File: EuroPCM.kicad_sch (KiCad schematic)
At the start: 1 part, among them IC1 TDA1541A

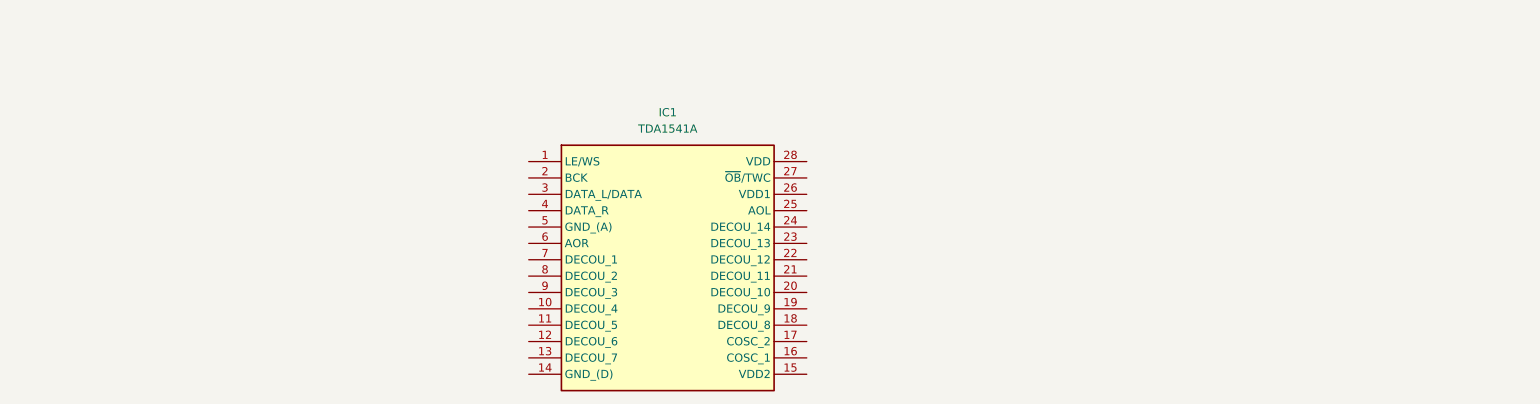
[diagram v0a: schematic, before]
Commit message: Add tda1315 footprint use schematic sheets
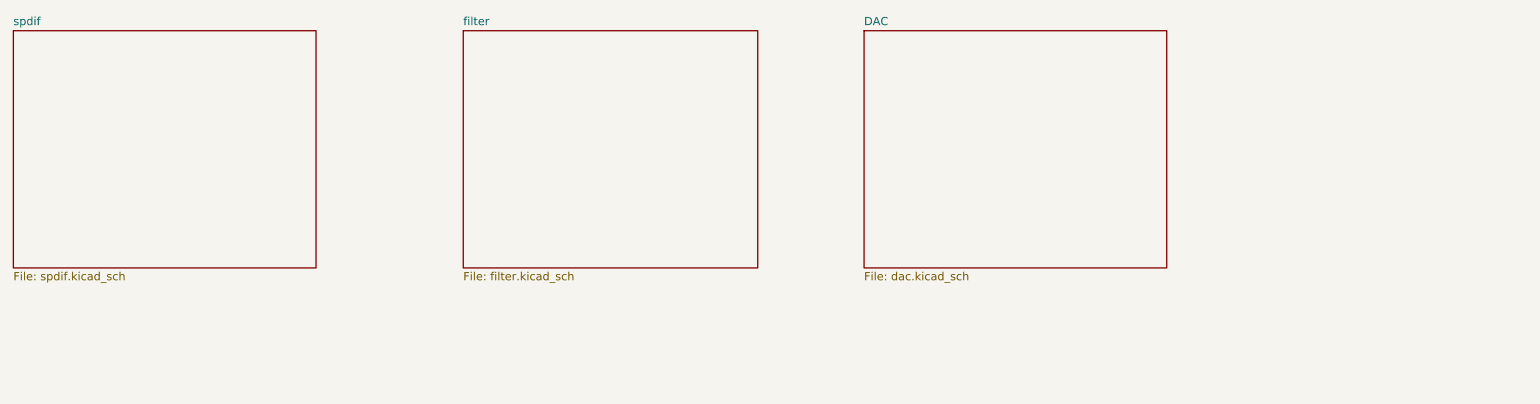
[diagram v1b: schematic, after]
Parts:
- removed IC1: TDA1541A, DIP1652W53P254L3550H510Q28N, symbol tda1541:TDA1541A
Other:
- added sheet DAC (dac.kicad_sch)
- added sheet filter (filter.kicad_sch)
- added sheet spdif (spdif.kicad_sch)
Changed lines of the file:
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@@
 	(generator_version "9.0")
 	(paper "A4")
-	(symbol
-		(lib_id "tda1541:TDA1541A")
-		(at 119.38 77.47 0)
-		(unit 1)
+	(sheet
+		(at 171.45 57.15)
+		(size 46.99 36.83)
 		(exclude_from_sim no)
 		(in_bom yes)
@@
 		(dnp no)
 		(fields_autoplaced yes)
-		(property "Reference" "IC1"
-			(at 140.97 69.85 0)
+		(stroke
+			(width 0.1524)
+			(type solid)
+		)
+		(fill
+			(color 0 0 0 0.0000)
+		)
+		(property "Sheetname" "DAC"
+			(at 171.45 56.4384 0)
 			(effects
 				(font
 					(size 1.27 1.27)
 				)
+				(justify left bottom)
 			)
 		)
-		(property "Value" "TDA1541A"
-			(at 140.97 72.39 0)
-			(effects
-				(font
-					(size 1.27 1.27)
-				)
-			)
-		)
-		(property "Footprint" "DIP1652W53P254L3550H510Q28N"
-			(at 158.75 172.39 0)
+		(property "Sheetfile" "dac.kicad_sch"
+			(at 171.45 94.5646 0)
 			(effects
 				(font
@@
 				)
 				(justify left top)
-				(hide yes)
 			)
 		)
-		(property "Datasheet" "http://lampizator.eu/LAMPIZATOR/LINKS%20AND%20DOWNLOADS/DATAMINING/tda%201541A.pdf"
-			(at 158.75 272.39 0)
+		(instances
+			(project "EuroPCM"
+				(path "/e63e39d7-6ac0-4ffd-8aa3-1841a4541b55"
+					(page "3")
+				)
+			)
+		)
+	)
+	(sheet
+		(at 109.22 57.15)
+		(size 45.72 36.83)
+		(exclude_from_sim no)
+		(in_bom yes)
+		(on_board yes)
+		(dnp no)
+		(fields_autoplaced yes)
+		(stroke
+			(width 0.1524)
+			(type solid)
+		)
+		(fill
+			(color 0 0 0 0.0000)
+		)
+		(property "Sheetname" "filter"
+			(at 109.22 56.4384 0)
+			(effects
+				(font
+					(size 1.27 1.27)
+				)
+				(justify left bottom)
+			)
+		)
+		(property "Sheetfile" "filter.kicad_sch"
+			(at 109.22 94.5646 0)
 			(effects
 				(font
@@
 				)
 				(justify left top)
-				(hide yes)
 			)
 		)
-		(property "Description" "Stereo high performance 16-bit DAC"
-			(at 119.38 77.47 0)
+		(instances
+			(project "EuroPCM"
+				(path "/e63e39d7-6ac0-4ffd-8aa3-1841a4541b55"
+					(page "4")
+				)
+			)
+		)
+	)
+	(sheet
+		(at 39.37 57.15)
+		(size 46.99 36.83)
+		(exclude_from_sim no)
+		(in_bom yes)
+		(on_board yes)
+		(dnp no)
+		(fields_autoplaced yes)
+		(stroke
+			(width 0.1524)
+			(type solid)
+		)
+		(fill
+			(color 0 0 0 0.0000)
+		)
+		(property "Sheetname" "spdif"
+			(at 39.37 56.4384 0)
 			(effects
 				(font
 					(size 1.27 1.27)
 				)
-				(hide yes)
+				(justify left bottom)
 			)
 		)
-		(property "Height" "5.1"
-			(at 158.75 472.39 0)
+		(property "Sheetfile" "spdif.kicad_sch"
+			(at 39.37 94.5646 0)
 			(effects
 				(font
@@
 				)
 				(justify left top)
-				(hide yes)
 			)
 		)
-		(property "Manufacturer_Name" "NXP"
-			(at 158.75 572.39 0)
-			(effects
-				(font
-					(size 1.27 1.27)
-				)
-				(justify left top)
-				(hide yes)
-			)
-		)
-		(property "Manufacturer_Part_Number" "TDA1541A"
-			(at 158.75 672.39 0)
-			(effects
-				(font
-					(size 1.27 1.27)
-				)
-				(justify left top)
-				(hide yes)
-			)
-		)
-		(property "Mouser Part Number" ""
-			(at 158.75 772.39 0)
-			(effects
-				(font
-					(size 1.27 1.27)
-				)
-				(justify left top)
-				(hide yes)
-			)
-		)
-		(property "Mouser Price/Stock" ""
-			(at 158.75 872.39 0)
-			(effects
-				(font
-					(size 1.27 1.27)
-				)
-				(justify left top)
-				(hide yes)
-			)
-		)
-		(property "Arrow Part Number" ""
-			(at 158.75 972.39 0)
-			(effects
-				(font
-					(size 1.27 1.27)
-				)
-				(justify left top)
-				(hide yes)
-			)
-		)
-		(property "Arrow Price/Stock" ""
-			(at 158.75 1072.39 0)
-			(effects
-				(font
-					(size 1.27 1.27)
-				)
-				(justify left top)
-				(hide yes)
-			)
-		)
-		(pin "9"
-		)
-		(pin "19"
-		)
-		(pin "26"
-		)
-		(pin "22"
-		)
-		(pin "21"
-		)
-		(pin "20"
-		)
-		(pin "8"
-		)
-		(pin "28"
-		)
-		(pin "23"
-		)
-		(pin "5"
-		)
-		(pin "25"
-		)
-		(pin "7"
-		)
-		(pin "11"
-		)
-		(pin "14"
-		)
-		(pin "13"
-		)
-		(pin "10"
-		)
-		(pin "18"
-		)
-		(pin "17"
-		)
-		(pin "16"
-		)
-		(pin "15"
-		)
-		(pin "3"
-		)
-		(pin "2"
-		)
-		(pin "1"
-		)
-		(pin "27"
-		)
-		(pin "12"
-		)
-		(pin "6"
-		)
-		(pin "4"
-		)
-		(pin "24"
-		)
 		(instances
-			(project ""
+			(project "EuroPCM"
 				(path "/e63e39d7-6ac0-4ffd-8aa3-1841a4541b55"
-					(reference "IC1")
-					(unit 1)
+					(page "2")
 				)
 			)

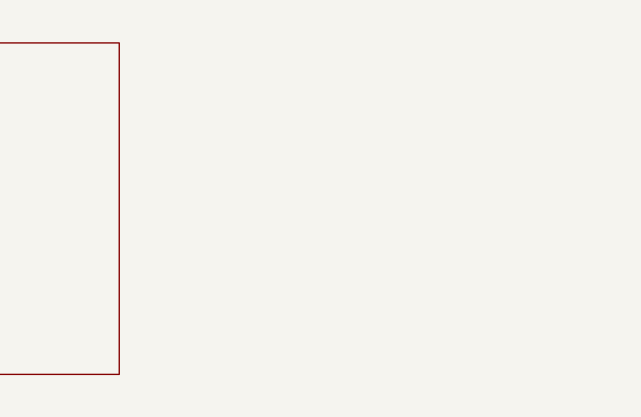
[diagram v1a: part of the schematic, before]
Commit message: Add amplifier circuit
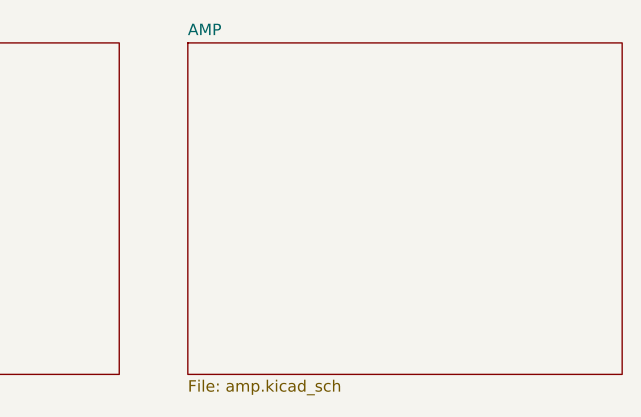
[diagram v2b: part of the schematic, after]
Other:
- added sheet AMP (amp.kicad_sch)
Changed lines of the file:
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@@
 	(paper "A4")
+	(sheet
+		(at 226.06 57.15)
+		(size 48.26 36.83)
+		(exclude_from_sim no)
+		(in_bom yes)
+		(on_board yes)
+		(dnp no)
+		(fields_autoplaced yes)
+		(stroke
+			(width 0.1524)
+			(type solid)
+		)
+		(fill
+			(color 0 0 0 0.0000)
+		)
+		(property "Sheetname" "AMP"
+			(at 226.06 56.4384 0)
+			(effects
+				(font
+					(size 1.27 1.27)
+				)
+				(justify left bottom)
+			)
+		)
+		(property "Sheetfile" "amp.kicad_sch"
+			(at 226.06 94.5646 0)
+			(effects
+				(font
+					(size 1.27 1.27)
+				)
+				(justify left top)
+			)
+		)
+		(instances
+			(project "EuroPCM"
+				(path "/e63e39d7-6ac0-4ffd-8aa3-1841a4541b55"
+					(page "5")
+				)
+			)
+		)
+	)
 	(sheet
 		(at 171.45 57.15)

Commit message: Progrees on spdif
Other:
- sheet filter renamed Filter
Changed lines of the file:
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@@
 			(project "EuroPCM"
 				(path "/e63e39d7-6ac0-4ffd-8aa3-1841a4541b55"
-					(page "3")
+					(page "4")
 				)
 			)
@@
 			(color 0 0 0 0.0000)
 		)
-		(property "Sheetname" "filter"
+		(property "Sheetname" "Filter"
 			(at 109.22 56.4384 0)
 			(effects
@@
 			(project "EuroPCM"
 				(path "/e63e39d7-6ac0-4ffd-8aa3-1841a4541b55"
-					(page "4")
+					(page "3")
 				)
 			)

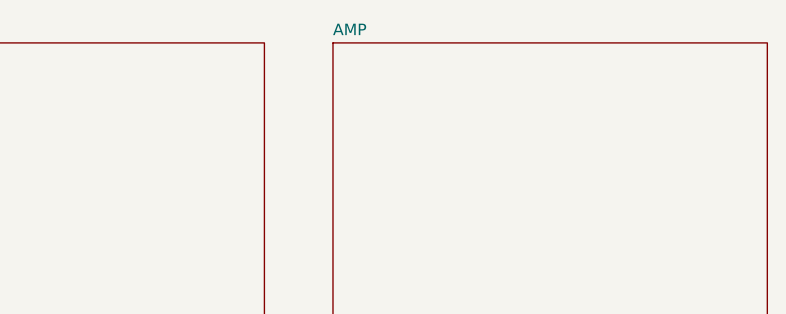
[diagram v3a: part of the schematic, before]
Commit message: Modify DEM circuit
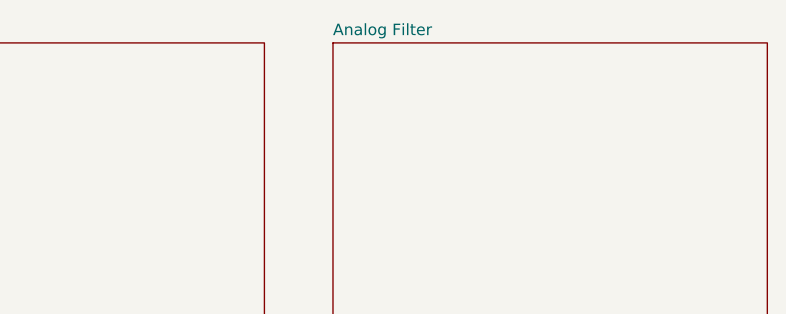
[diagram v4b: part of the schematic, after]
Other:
- sheet AMP renamed Analog Filter
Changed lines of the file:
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@@
 			(color 0 0 0 0.0000)
 		)
-		(property "Sheetname" "AMP"
+		(property "Sheetname" "Analog Filter"
 			(at 226.06 56.4384 0)
 			(effects
